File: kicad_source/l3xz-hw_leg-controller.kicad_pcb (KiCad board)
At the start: 2 copper layers, 178 x 29 mm, 57 parts, among them CN1 ARDUINO_NANO_33, CN2 SM04B-SRSS-TB, CN3 SM04B-SRSS-TB, CN4 GH_SM04B-GHS-TB, CN5 GH_SM04B-GHS-TB, CN6 691322310002, CN7 CONN_02X03, CN8 WAGO 733-362, U1 AS5048A, U2 AS5048A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

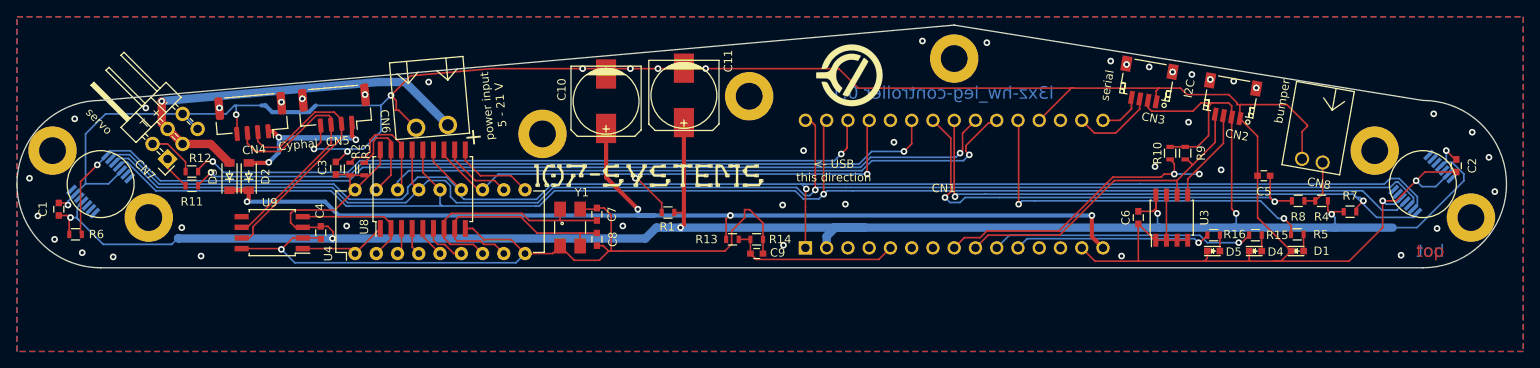
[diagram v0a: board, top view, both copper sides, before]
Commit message: fixed crystal issues, corrected CAN driver footprint, added pullup on MISO
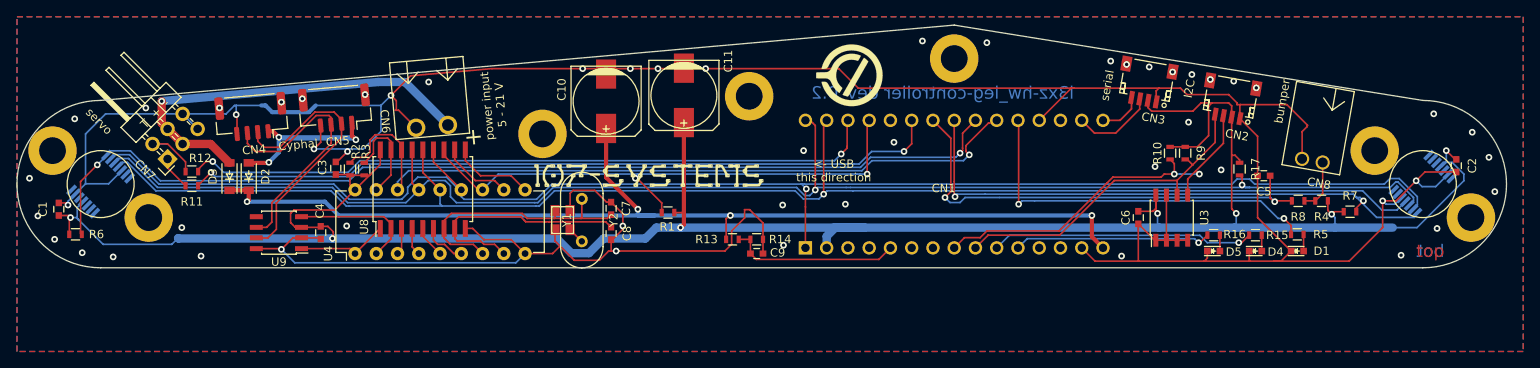
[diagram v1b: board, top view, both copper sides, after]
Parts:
- added R17: 10k, resistors:R_0603, F.Cu at (186.1, 88.2)
- added Y2: 16MHz, crystals:HC-49V, F.Cu at (107.5, 94.3)
- U9: footprint SOIC:SOIJ-8_5.3x5.3mm_Pitch1.27mm -> SOIC:SOIC-8_3.9x4.9mm_Pitch1.27mm
- Y1: footprint crystals:Crystal_SMD_0603_4Pads -> crystals:Crystal_SMD_3.2x2.5mm_4Pad
- moved C7 1.84 mm to (111.0, 92.9)
- moved C8 1.84 mm to (111.0, 95.9)
- moved Y1 1.27 mm to (105.2, 94.3), turned to 90 degrees
- moved U9 0.80 mm to (71.3, 95.8)
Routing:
- net GND: track 406.4 -> 411.5 mm, vias 45 -> 46
- net /MCP2515/MCP2515_OSC2: track 27.6 -> 31.4 mm
- net /MCP2515/MCP2515_OSC1: track 28.3 -> 31.6 mm
- net +3V3: track 283.3 -> 286.3 mm
- net MISO: track 178.6 -> 180.9 mm, vias 1 -> 2
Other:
- board text added: "l3xz-hw_leg-controller dev_0.2"
- board text removed: "l3xz-hw_leg-controller 0.1"

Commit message: updated images and schematic pdf
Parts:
- moved L1 4.12 mm to (119.1, 87.0)
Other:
- board text added: "L3XZ"
- board text added: "UCANPHY Micro"
- board text removed: "Cyphal"
